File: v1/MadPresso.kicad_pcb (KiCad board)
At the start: 2 copper layers, 108 x 57.5 mm, 67 parts, among them J1 Conn_01x07, J2 Conn_01x03, Q1 2N7002, Q2 2N7002, Q3 BC847, Q4 BT138-600, Q5 BT138-600, Q6 BT138-600, Q7 2N7002, Q8 2N7002, Q9 2N7002, U1 LTV-356T, U2 TLP160G, U3 TLP160G, U4 TLP160G, U5 MID400S, U6 MID400S, U7 WeMos_mini

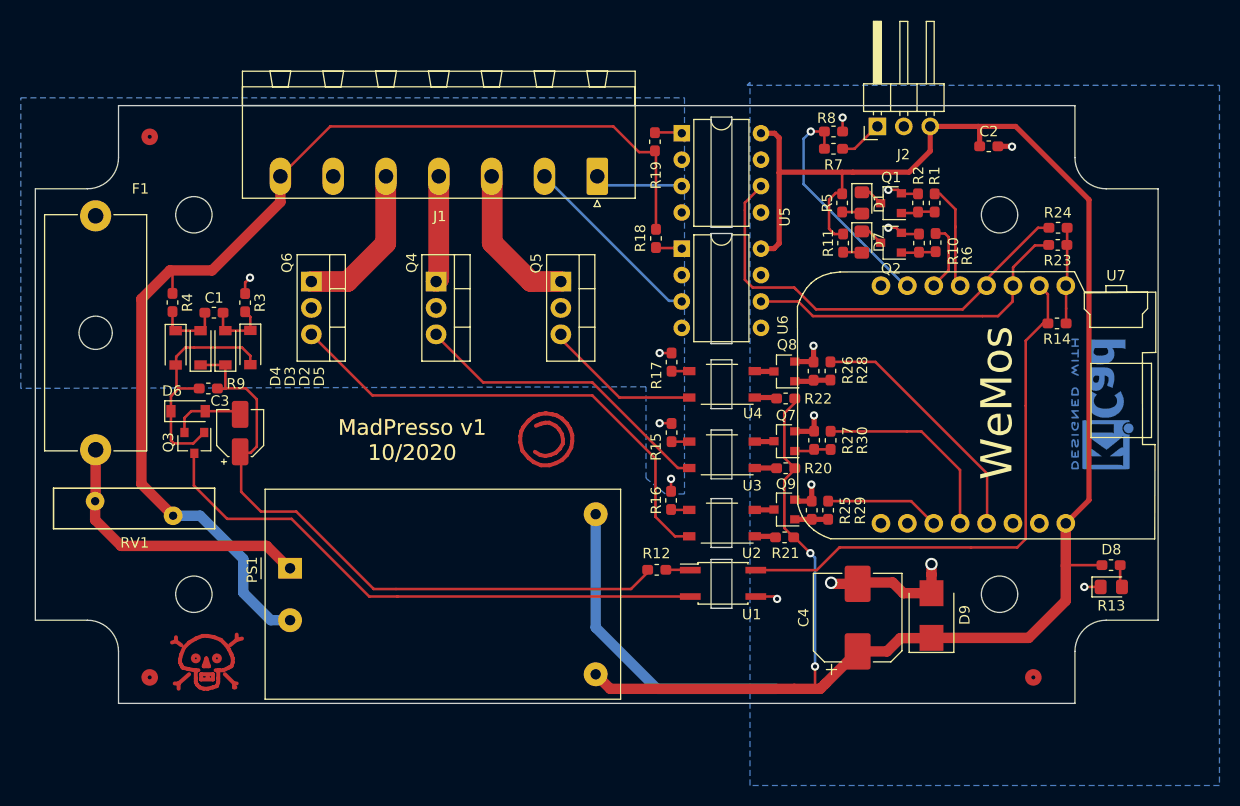
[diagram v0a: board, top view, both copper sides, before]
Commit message: Add another blocker C
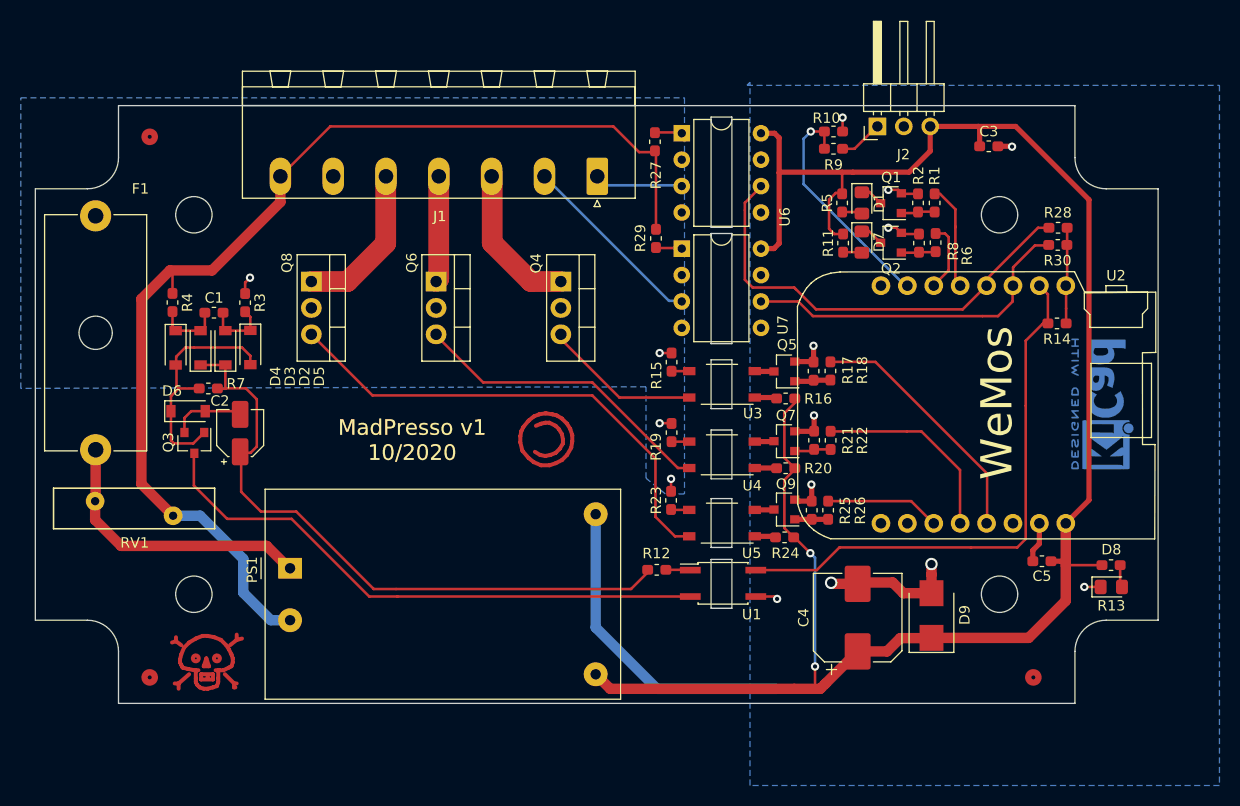
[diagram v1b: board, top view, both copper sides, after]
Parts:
- added C5: 1uF, Capacitor_SMD:C_0603_1608Metric_Pad1.05x0.95mm_HandSolder, F.Cu at (96.8, 43.8)
- R10: renamed from R8; value 91k -> DNP
- R9: renamed from R7; value 47k -> 0R
- renumbered C3 to C2, C2 to C3, Q5 to Q4, Q8 to Q5, Q4 to Q6, Q6 to Q8, R17 to R15, R22 to R16, R26 to R17, R28 to R18, R15 to R19, R27 to R21, R30 to R22, R16 to R23, R21 to R24, R29 to R26, R19 to R27, R24 to R28, R18 to R29, R23 to R30, R9 to R7, R10 to R8, U7 to U2, U4 to U3, U3 to U4, U2 to U5, U5 to U6, U6 to U7
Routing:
- net GND: track 66.5 -> 70.5 mm
- net +5V: track 182.1 -> 183.7 mm

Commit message: some resistor footpring changes
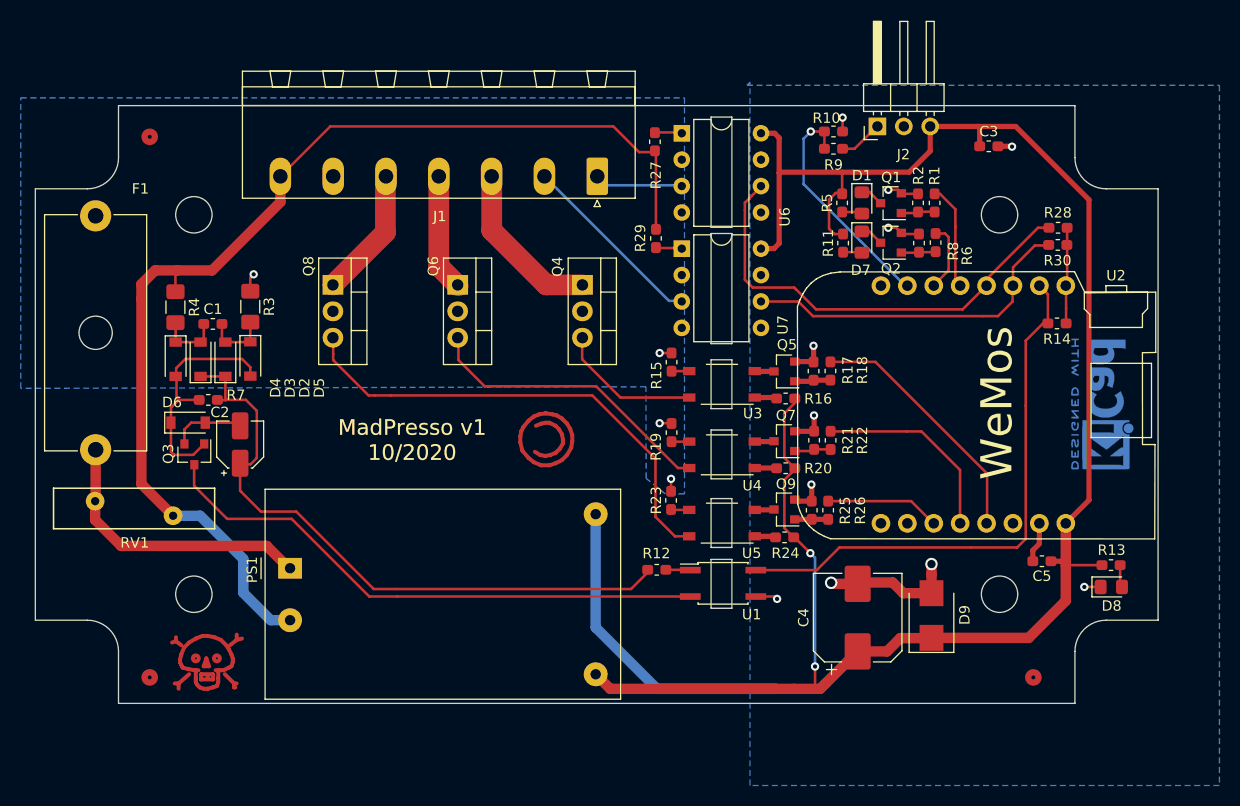
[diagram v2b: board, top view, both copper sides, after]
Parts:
- R11, R13, R5: value 220 -> 330
- R3, R4: footprint Resistor_SMD:R_0603_1608Metric_Pad1.05x0.95mm_HandSolder -> Resistor_SMD:R_1206_3216Metric_Pad1.42x1.75mm_HandSolder
- moved Q4 2.10 mm to (52.6, 17.2)
- moved Q6 2.10 mm to (40.6, 17.2)
- moved Q8 2.10 mm to (28.6, 17.2)
- moved C2 1.10 mm to (19.7, 32.6)
- moved D2 1.10 mm to (18.3, 24.4)
- moved D3 1.10 mm to (15.9, 24.4)
- moved D4 1.10 mm to (13.5, 24.4)
- moved D5 1.10 mm to (20.7, 24.4)
- moved D6 1.10 mm to (14.7, 30.5)
- moved R7 1.10 mm to (16.6, 28.3)
- moved Q3 1.10 mm to (15.3, 33.5)
- moved C1 1.09 mm to (17.1, 21.0)
- moved R3 0.63 mm to (20.7, 19.3)
- moved R4 0.53 mm to (13.5, 19.4)
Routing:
- net /VALVE: track 15.6 -> 13.1 mm
- net /HEATER: track 14.9 -> 16.7 mm
- net Net-(Q3-Pad3): track 55.3 -> 54.2 mm
- net Net-(Q6-Pad3): track 30.1 -> 29.1 mm
- net Net-(Q8-Pad3): track 47.7 -> 46.8 mm
- net Net-(C2-Pad1): track 62.9 -> 62.0 mm
- net Net-(Q4-Pad3): track 15.2 -> 14.3 mm
- net /PUMP: track 10.5 -> 11.3 mm
- net Net-(C1-Pad1): track 6.23 -> 5.56 mm
- net NEUT: track 108.1 -> 108.8 mm

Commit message: more work
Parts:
- F1: value 1A/250V -> 0.1A/250V
- moved R30 1.10 mm to (98.4, 14.5)
- moved R28 1.10 mm to (98.4, 12.8)
- moved R7 0.34 mm to (16.3, 28.3)
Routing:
- net /HEATER: track 16.7 -> 17.8 mm
- net /VALVE: track 13.1 -> 12.0 mm
- net VCC: track 9.64 -> 8.66 mm
- net /STEAM_SENSOR: track 34.0 -> 33.0 mm
- net /PUMP: track 11.3 -> 10.7 mm
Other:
- board text added: "MadPresso v1 11/2020"
- board text removed: "MadPresso v1 10/2020"

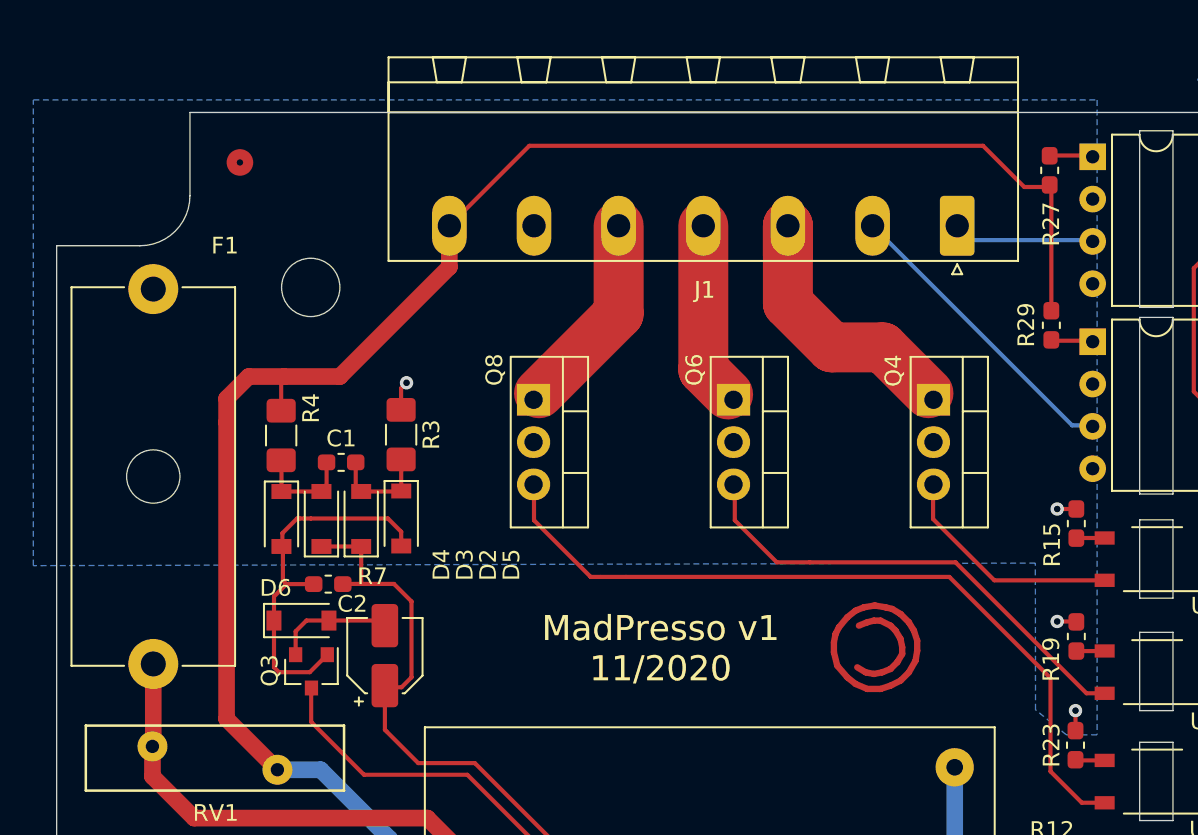
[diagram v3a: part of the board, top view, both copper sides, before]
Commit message: mirror power traces on bottom layer
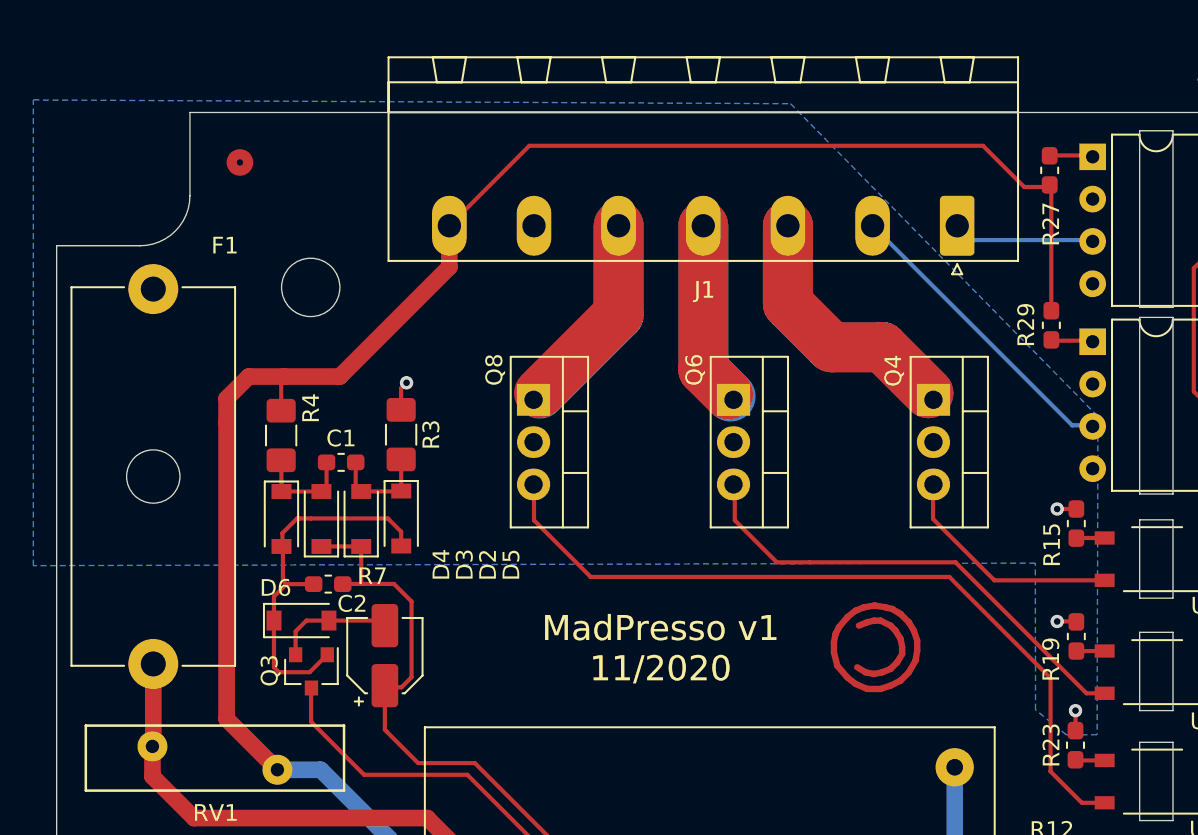
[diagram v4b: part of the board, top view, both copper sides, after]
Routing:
- net /HEATER: track 17.8 -> 33.2 mm
- net /VALVE: track 12.0 -> 24.1 mm
- net /PUMP: track 10.7 -> 21.7 mm
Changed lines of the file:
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@@
   (segment (start 49.575 14.1) (end 52.325 16.85) (width 3) (layer "F.Cu") (net 7))
   (segment (start 52.625 17.245) (end 52.545 17.245) (width 2) (layer "F.Cu") (net 7))
+  (segment (start 43.89 6.8) (end 43.89 11.49) (width 3) (layer "B.Cu") (net 7))
+  (segment (start 43.89 11.49) (end 46.475 14.075) (width 3) (layer "B.Cu") (net 7))
+  (segment (start 46.475 14.075) (end 49.55 14.075) (width 3) (layer "B.Cu") (net 7))
+  (segment (start 49.55 14.075) (end 52.325 16.85) (width 3) (layer "B.Cu") (net 7))
   (segment (start 38.81 6.8) (end 38.81 15.435) (width 3) (layer "F.Cu") (net 8))
   (segment (start 38.81 15.435) (end 40.3 16.925) (width 3) (layer "F.Cu") (net 8))
+  (segment (start 38.81 6.8) (end 38.81 15.41) (width 3) (layer "B.Cu") (net 8))
+  (segment (start 38.81 15.41) (end 40.45 17.05) (width 3) (layer "B.Cu") (net 8))
   (segment (start 32.12 47.22) (end 24.65 39.75) (width 0.25) (layer "F.Cu") (net 9))
   (segment (start 34.82 47.22) (end 32.12 47.22) (width 0.25) (layer "F.Cu") (net 9))
@@
   (segment (start 33.73 6.8) (end 33.73 12.07) (width 3) (layer "F.Cu") (net 19))
   (segment (start 33.73 12.07) (end 28.95 16.85) (width 3) (layer "F.Cu") (net 19))
+  (segment (start 33.73 6.8) (end 33.73 12.145) (width 3) (layer "B.Cu") (net 19))
+  (segment (start 33.73 12.145) (end 29 16.875) (width 3) (layer "B.Cu") (net 19))
   (segment (start 71.21 28.08) (end 71.3 28.17) (width 0.5) (layer "F.Cu") (net 20))
   (segment (start 69.2 28.08) (end 71.21 28.08) (width 0.5) (layer "F.Cu") (net 20))
@@
     (polygon
       (pts
+        (xy 62.5 18.25)
         (xy 62.443848 37.35)
         (xy 60.596924 37.35)
@@
         (xy -1.4 27.2)
         (xy -1.4 -0.75)
-        (xy 62.443848 -0.75)
+        (xy 44.05 -0.525)
       )
     )

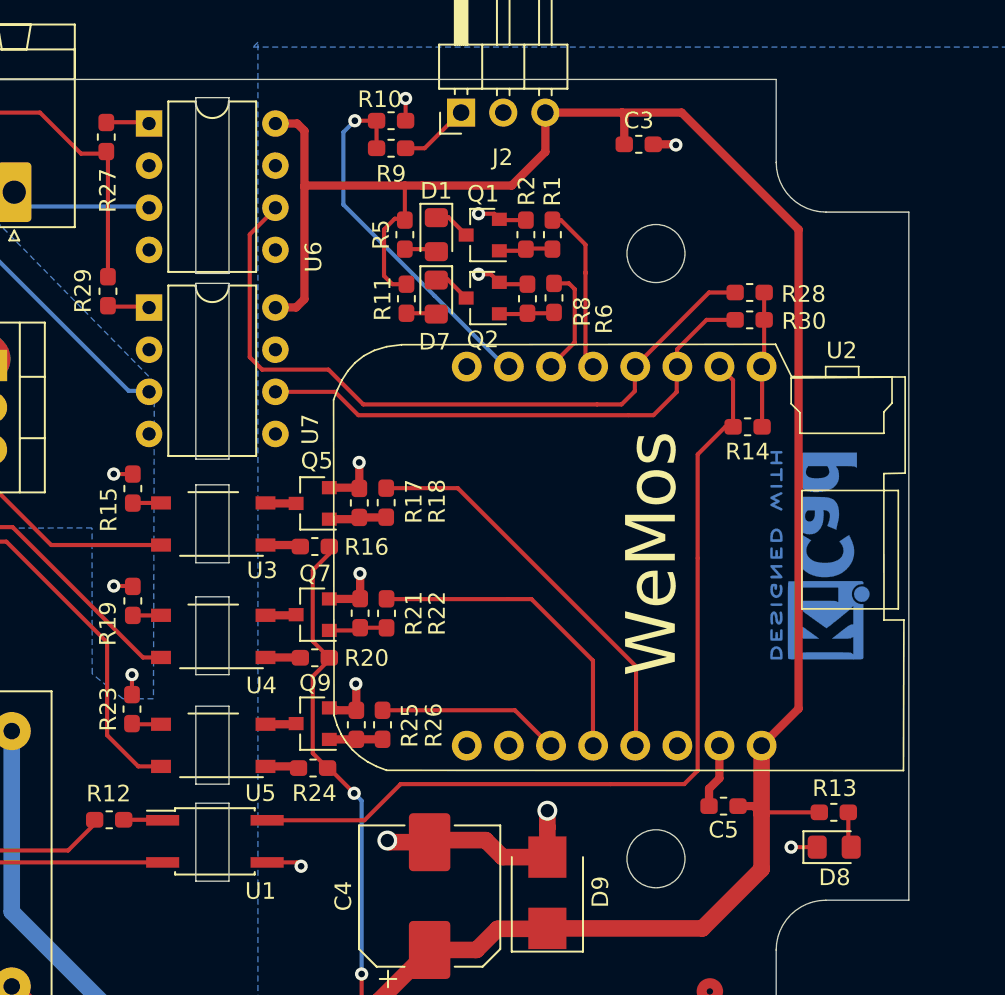
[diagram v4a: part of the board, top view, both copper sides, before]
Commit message: Update to new KiCad symbols, replace and turn D1 module
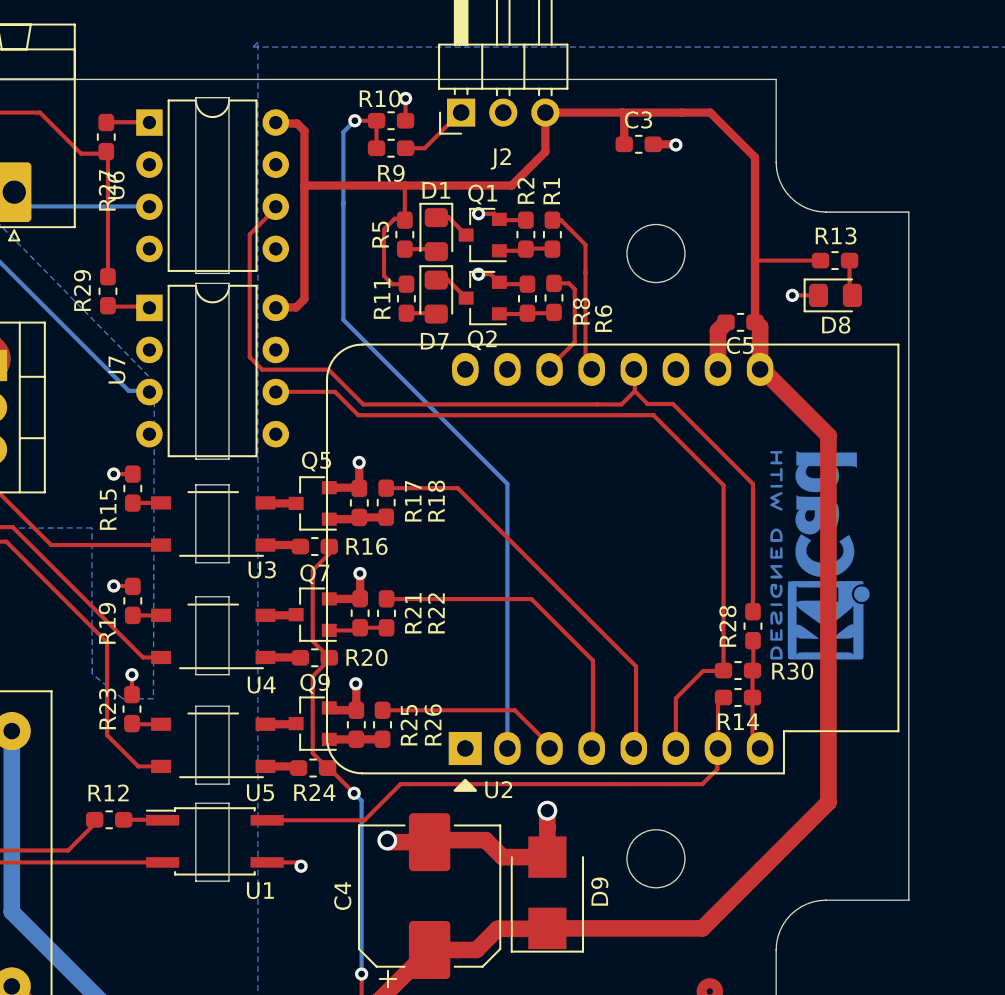
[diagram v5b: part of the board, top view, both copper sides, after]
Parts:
- U2: value WeMos_mini -> WeMos_D1_mini; footprint wemos_d1_mini:D1_mini_board -> Module:WEMOS_D1_mini_light
- U6, U7: value MID400S -> MID400
- moved R13 33.3 mm to (103.5, 10.9)
- moved D8 33.3 mm to (103.6, 13.0)
- moved C5 29.2 mm to (97.8, 14.7)
- moved R30 21.2 mm to (97.7, 35.6)
- moved R28 20.1 mm to (98.6, 33.0), turned to 90 degrees
- moved R14 16.3 mm to (97.7, 37.3)
- moved U2 15.5 mm to (81.2, 40.4)
- moved U6 0.06 mm to (62.2, 2.60)
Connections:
- U2 pad 1: +5V -> (no net)
- U2 pad 10: /TEMP_SENSOR -> GND
- U2 pad 11: /LED2 -> (no net)
- U2 pad 12: /LED1 -> /SHOT_SENSOR
- U2 pad 13: /SHOT_SENSOR -> /LED1
- U2 pad 14: /STEAM_SENSOR -> /LED2
- U2 pad 15: /ZC_DETECT -> (no net)
- U2 pad 16: VCC -> (no net)
- U2 pad 2: GND -> /TEMP_SENSOR
- U2 pad 3: (no net) -> /VALVE_TRIAC
- U2 pad 4: /HEATER_TRIAC -> /PUMP_TRIAC
- U2 pad 5: /PUMP_TRIAC -> /HEATER_TRIAC
- U2 pad 6: /VALVE_TRIAC -> /STEAM_SENSOR
- U2 pad 7: (no net) -> /ZC_DETECT
- U2 pad 8: (no net) -> VCC
- U2 pad 9: (no net) -> +5V
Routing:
- net /TEMP_SENSOR: track 22.6 -> 45.5 mm
- net /ZC_DETECT: track 53.1 -> 33.0 mm
- net /STEAM_SENSOR: track 33.0 -> 47.2 mm
- net /SHOT_SENSOR: track 43.8 -> 53.0 mm
- net +5V: track 183.7 -> 185.9 mm
- net VCC: track 8.66 -> 6.73 mm
- net GND: track 70.5 -> 69.5 mm

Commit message: cleanups
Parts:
- moved D1 0.75 mm to (79.5, 8.61)
- moved D7 0.75 mm to (79.5, 12.4)
- moved Q1 0.75 mm to (82.3, 8.63)
- moved Q2 0.75 mm to (82.3, 12.4)
- moved R1 0.75 mm to (86.5, 8.61)
- moved R11 0.75 mm to (77.7, 12.5)
- moved R2 0.75 mm to (84.9, 8.61)
- moved R5 0.75 mm to (77.6, 8.61)
- moved R6 0.75 mm to (86.6, 12.4)
- moved R8 0.75 mm to (85.0, 12.5)
- moved R27 0.13 mm to (59.7, 3.55)
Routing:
- net /STEAM_SW: track 18.2 -> 21.3 mm
- net /LED1: track 10.2 -> 11.4 mm
- net /LED2: track 6.72 -> 7.47 mm
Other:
- outline, holes or cut-outs redrawn
